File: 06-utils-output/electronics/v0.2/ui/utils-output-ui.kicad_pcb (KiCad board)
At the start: 2 copper layers, 58 x 110 mm, 34 parts, among them J1 Conn_02x03_Odd_Even, J2 Conn_02x04_Odd_Even, J3 Conn_02x02_Odd_Even, J4 Conn_01x02, J5 Conn_01x06, J6 Conn_02x05_Odd_Even, Q1 2N3904

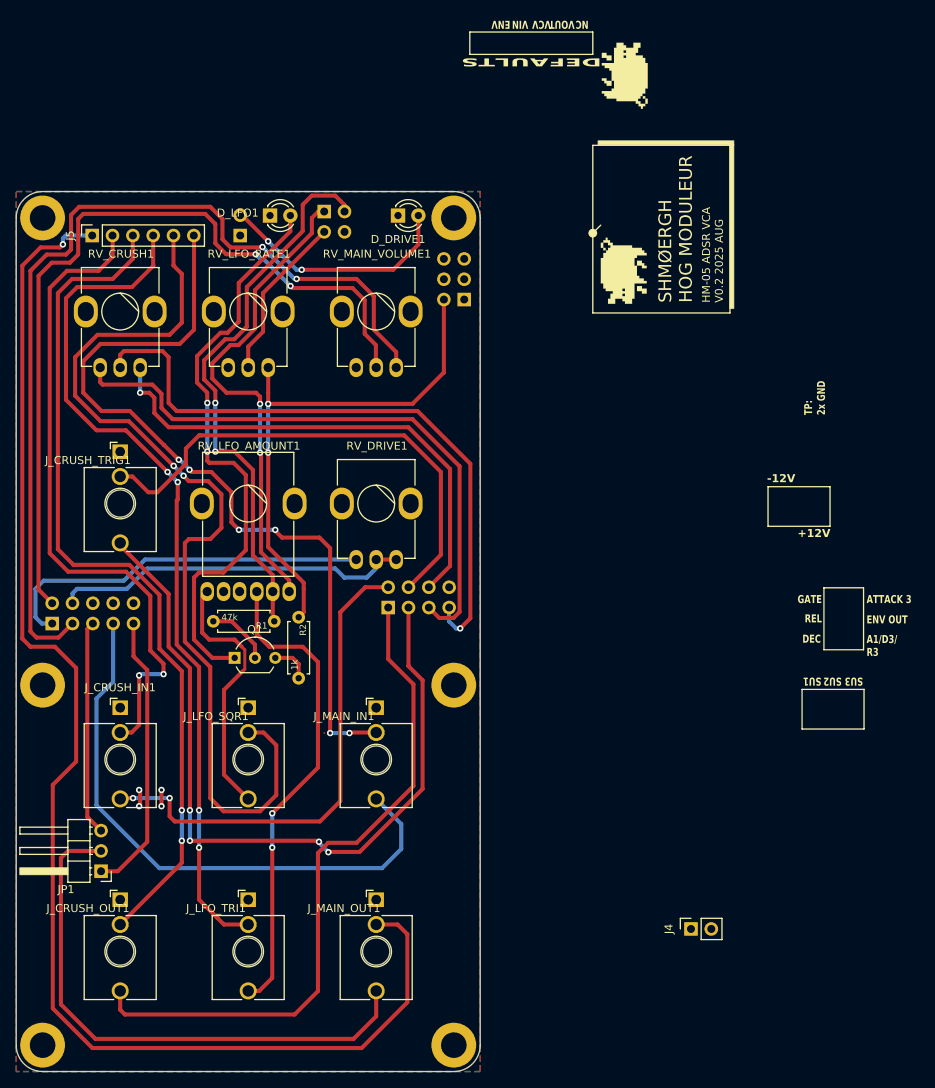
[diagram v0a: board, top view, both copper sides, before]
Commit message: Redesigned utils + output UI PCB
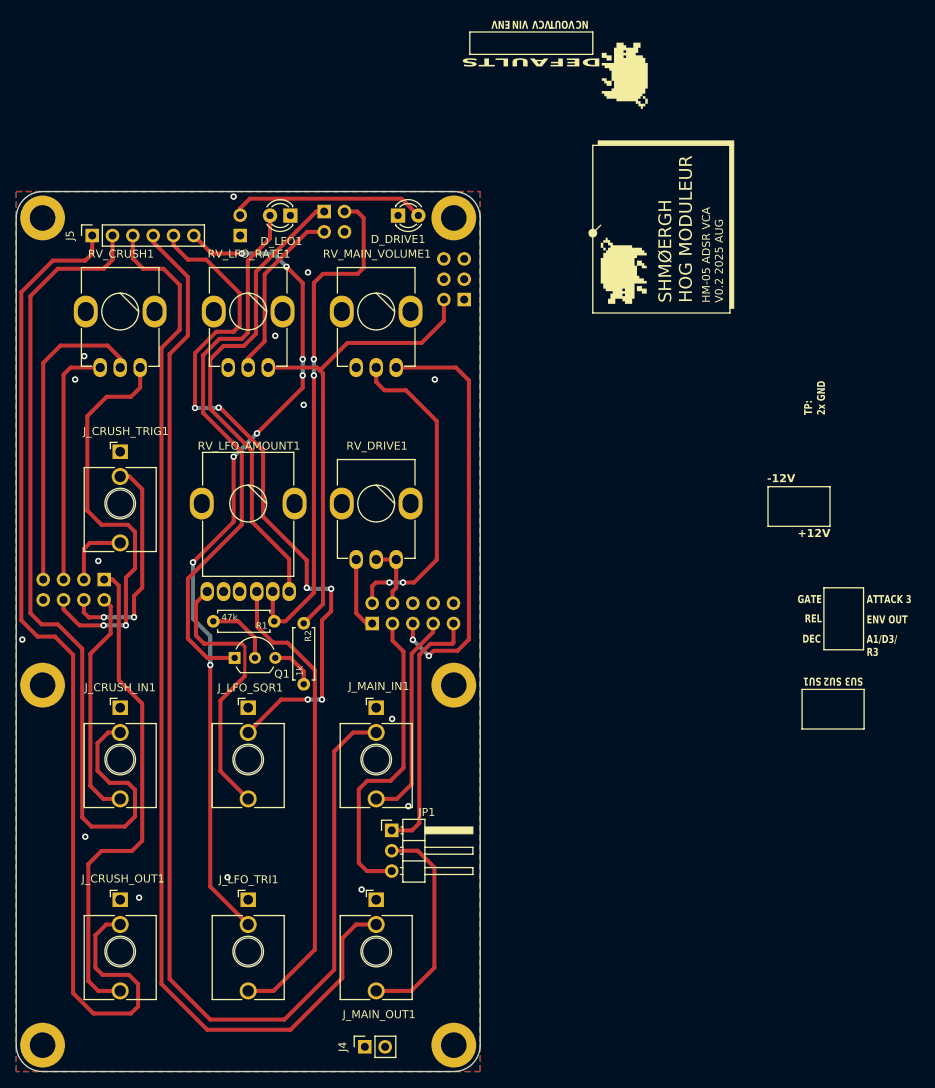
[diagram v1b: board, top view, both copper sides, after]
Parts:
- moved J4 43.3 mm to (167.6, 150.9)
- moved J6 40.0 mm to (168.5, 98.0)
- moved JP1 36.7 mm to (170.9, 123.9), turned to 0 degrees
- moved J2 35.7 mm to (135.0, 92.5), turned to 90 degrees
- moved D_LFO1 2.54 mm to (158.3, 47.0), turned to 180 degrees
- moved R2 0.99 mm to (159.9, 98.0)
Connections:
- J5 pad 1: OUTPUT_OUT_DEFAULT -> CRUSH_OUT_DEFAULT
- J5 pad 3: CRUSH_OUT_DEFAULT -> OUTPUT_OUT_DEFAULT
- J5 pad 4: LFO_TRI_DEFAULT -> OUTPUT_IN_DEFAULT
- J5 pad 6: OUTPUT_IN_DEFAULT -> LFO_TRI_DEFAULT
- J6 pad 3: OUTPUT_VOL_3 -> OUTPUT_PHONES_OUT
- J6 pad 5: OUTPUT_PHONES_OUT -> OUTPUT_VOL_3
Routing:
- net CRUSH_TRIG: track 97.3 -> 8.68 mm, vias 4 -> 0
- net OUTPUT_VOL_3: track 116.4 -> 52.9 mm
- net OUTPUT_VOL_2: track 103.1 -> 40.3 mm
- net OUTPUT_IN_DEFAULT: track 101.3 -> 154.5 mm, vias 6 -> 0
- net OUTPUT_IN: track 73.5 -> 26.4 mm
- net RV_CRUSH_1: track 75.1 -> 30.6 mm
- net OUTPUT_OUT: track 69.2 -> 27.2 mm
- net RV_CRUSH_2: track 79.3 -> 39.4 mm, vias 1 -> 0
- net OUTPUT_DRIVE_1: track 47.6 -> 9.24 mm
- net OUTPUT_DRIVE_3: track 45.0 -> 8.15 mm
- net OUTPUT_OUT_DEFAULT: track 171.0 -> 136.0 mm, vias 1 -> 0
- net CRUSH_TRIG_DEFAULT: track 62.9 -> 27.9 mm, vias 0 -> 2
- net CRUSH_IN: track 62.1 -> 29.0 mm, vias 2 -> 0
- net LFO_SQR_DEFAULT: track 117.6 -> 88.4 mm, vias 2 -> 6
- net CRUSH_IN_DEFAULT: track 82.6 -> 107.6 mm, vias 2 -> 0
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
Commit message: Added minimum resistance to LFO CV
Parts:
- added R3: 150-220, Shmoergh_Custom_Footprints:R_Axial_DIN0207_L6.3mm_D2.5mm_P7.62mm_Horizontal, F.Cu at (157.0, 70.3)
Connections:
- RV_LFO_RATE1 pad 1: GND -> Net-(R3-Pad1)
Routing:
- net Net-(R3-Pad1): track 0.00 -> 9.89 mm
- net LFO_TRI_DEFAULT: track 104.8 -> 107.3 mm
- net GND: vias 15 -> 16

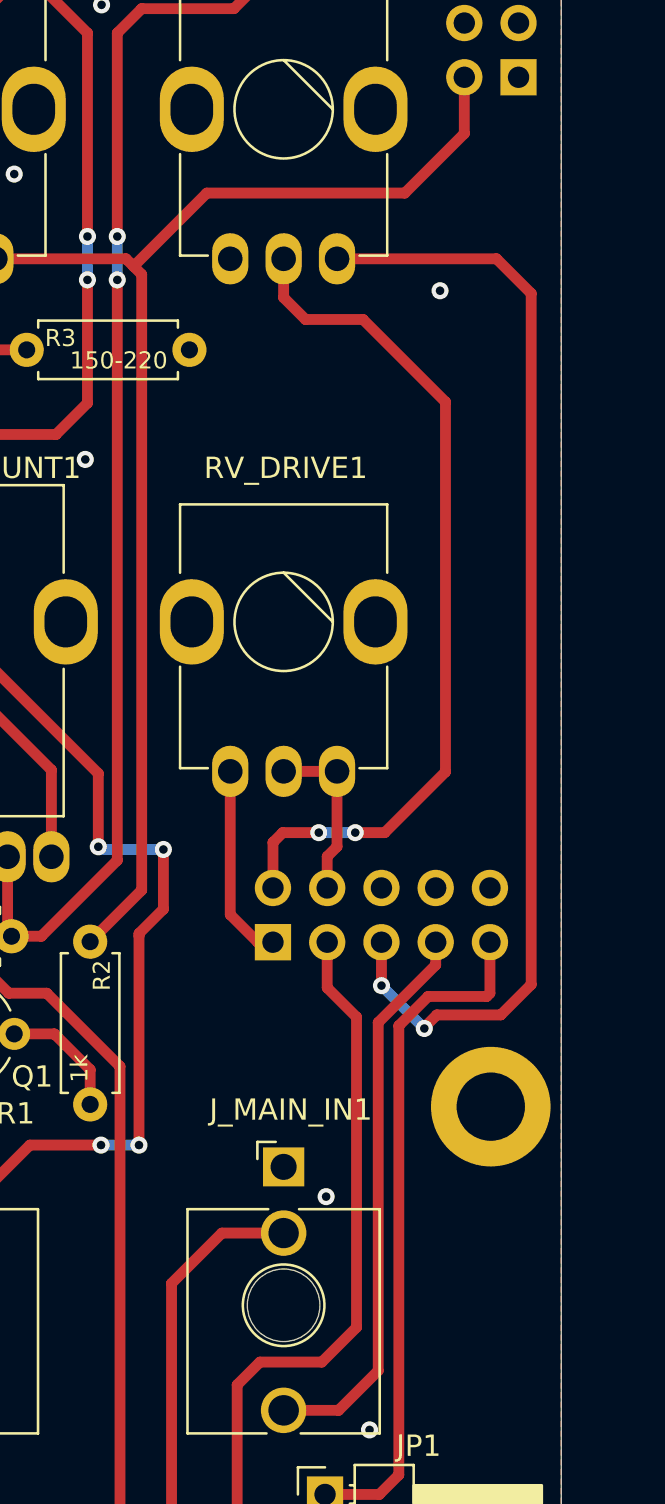
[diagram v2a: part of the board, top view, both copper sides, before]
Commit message: Redesigned output module
- The master volume was _before_ the gain control which made no sense because the volume had an effect on how much signal went into the gain stage. Now the master volume is after the diode limiter/clamper which means the output can be tamed while keeping the overdrive.
- Rearranged the output resistors so now line out has a 1k resistor.
- STILL TODO: the headphone output is not protected against accidental +/-12V inputs.
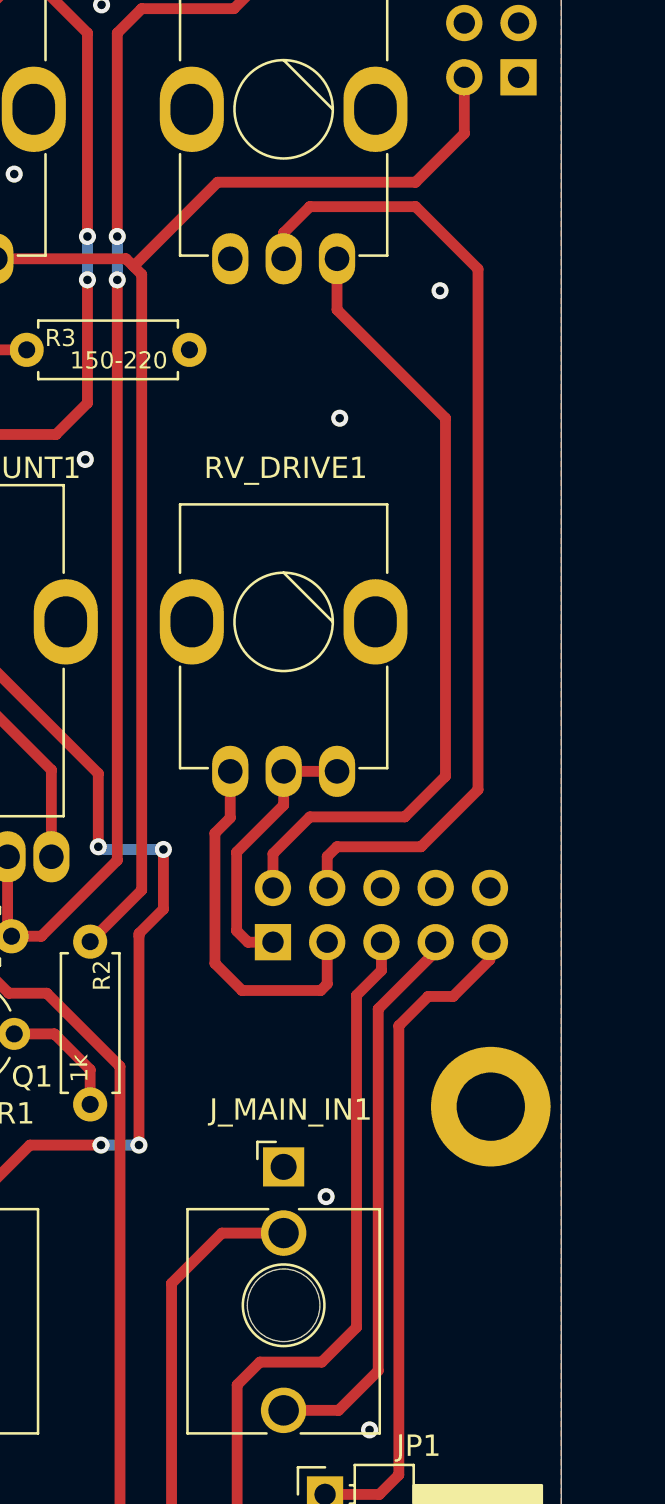
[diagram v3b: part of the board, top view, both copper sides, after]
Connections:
- J6 pad 1: OUTPUT_DRIVE_1 -> OUTPUT_DRIVE_3
- J6 pad 2: OUTPUT_VOL_2 -> OUTPUT_VOL_3
- J6 pad 3: OUTPUT_PHONES_OUT -> OUTPUT_DRIVE_1
- J6 pad 4: OUTPUT_DRIVE_3 -> OUTPUT_VOL_2
- J6 pad 5: OUTPUT_VOL_3 -> OUTPUT_PHONES_OUT
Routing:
- net OUTPUT_VOL_3: track 52.9 -> 37.5 mm, vias 2 -> 0
- net OUTPUT_DRIVE_1: track 9.24 -> 17.2 mm
- net OUTPUT_VOL_2: track 40.3 -> 46.2 mm, vias 2 -> 0
- net OUTPUT_DRIVE_3: track 8.15 -> 12.8 mm
- net OUTPUT_LINE_OUT: track 32.2 -> 31.2 mm
- net GND: vias 16 -> 17
